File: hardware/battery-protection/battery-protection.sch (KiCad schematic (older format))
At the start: 20 parts, among them J1 M6 Battery input, J2 M5 Ground, J3 M5 Output, J4 M5 Output, J5 M5 Output, Q1 Q_PMOS_SGD, Q2 Q_PMOS_SGD, Q3 Q_PMOS_SGD, Q4 Q_PMOS_SGD, Q5 Q_PMOS_SGD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

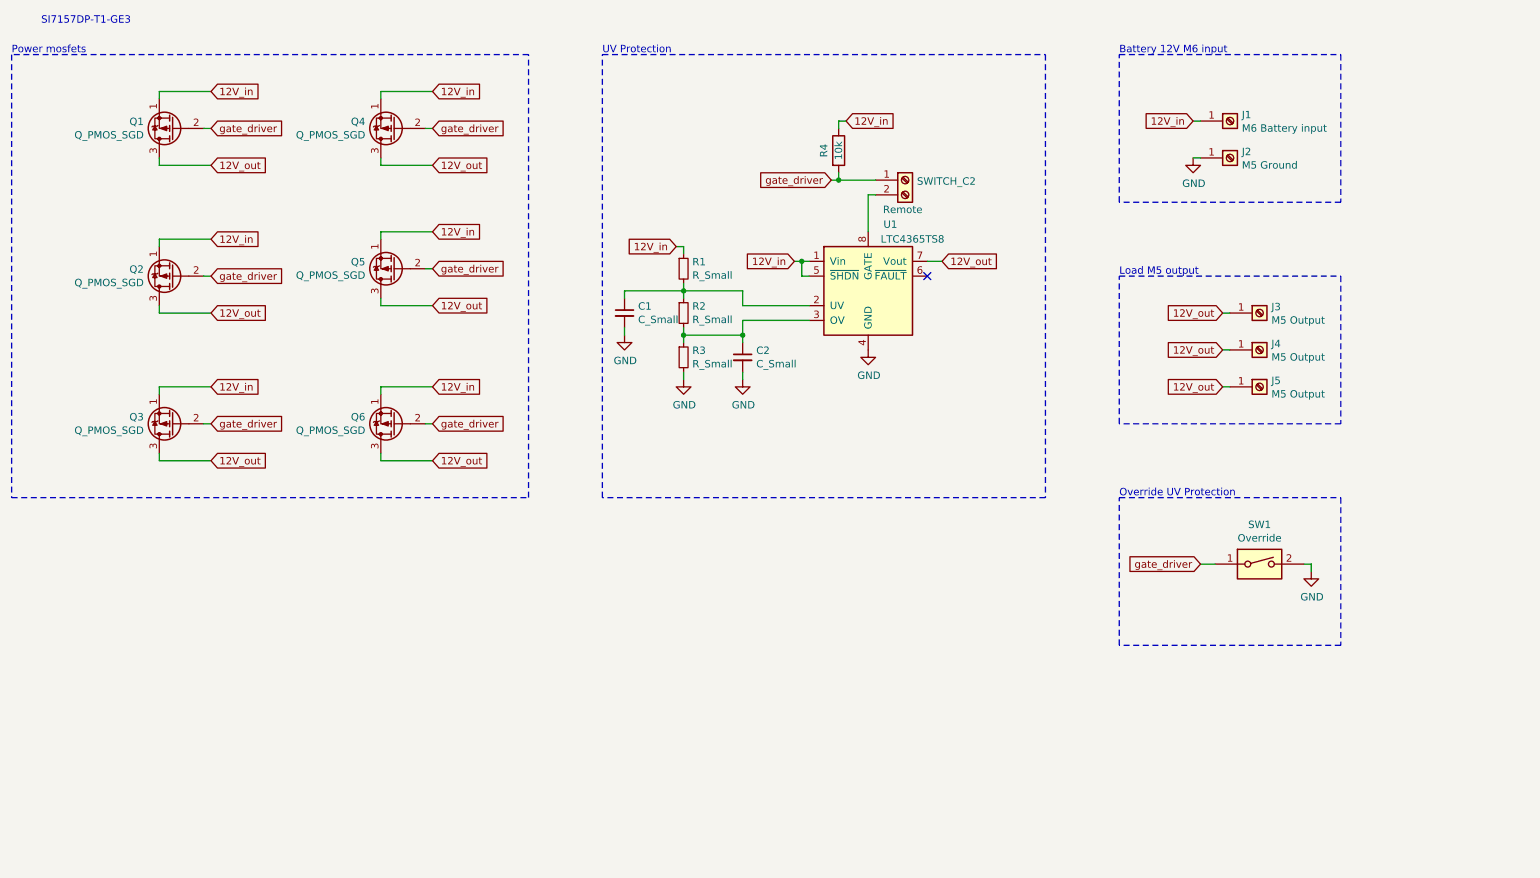
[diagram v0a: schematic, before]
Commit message: Finished routing battery protection
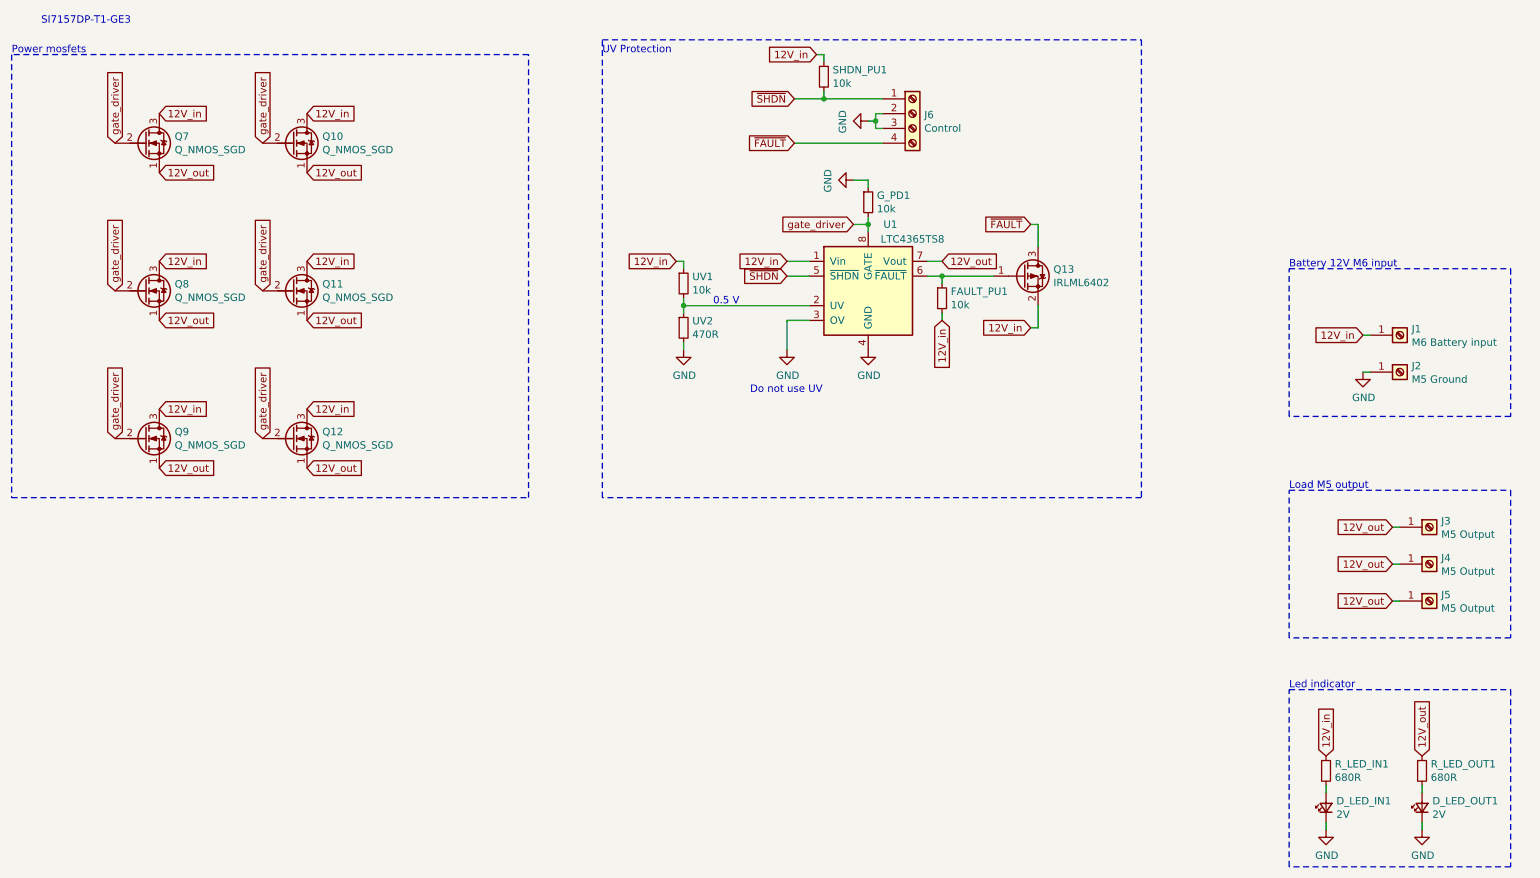
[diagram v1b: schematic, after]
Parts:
- removed C1, C2: C_Small, Capacitor_SMD:C_0603_1608Metric, symbol Device:C_Small
- removed Q1, Q2, Q3, Q4, Q5, Q6: Q_PMOS_SGD, mosfet:POWERPAKSO-8, symbol Device:Q_PMOS_SGD
- removed R3: R_Small, Resistor_SMD:R_0603_1608Metric, symbol Device:R_Small
- removed R4: 10k, Resistor_SMD:R_0603_1608Metric, symbol Device:R
- removed SW1: Override, symbol Switch:SW_DIP_x01
- removed SWITCH_C2: Remote, TerminalBlock_Phoenix:TerminalBlock_Phoenix_PT-1,5-2-5.0-H_1x02_P5.00mm_Horizontal, symbol Connector:Screw_Terminal_01x02
- added D_LED_IN1, D_LED_OUT1: 2V, LED_SMD:LED_0603_1608Metric, symbol Device:LED_Small
- added FAULT_PU1, G_PD1, SHDN_PU1: 10k, Resistor_SMD:R_0603_1608Metric, symbol Device:R_Small
- added J6: Control, TerminalBlock_Phoenix:TerminalBlock_Phoenix_MKDS-1,5-4_1x04_P5.00mm_Horizontal, symbol Connector:Screw_Terminal_01x04
- added Q10, Q11, Q12, Q7, Q8, Q9: Q_NMOS_SGD, mosfet:SQJA72EPT1_GE3, symbol Device:Q_NMOS_SGD
- added Q13: IRLML6402, Package_TO_SOT_SMD:SOT-23, symbol Transistor_FET:IRLML6402
- added R_LED_IN1, R_LED_OUT1: 680R, Resistor_SMD:R_0603_1608Metric, symbol Device:R_Small
- U1: footprint (none) -> Package_TO_SOT_SMD:SOT-23-8
- UV1: renamed from R1; value R_Small -> 10k
- UV2: renamed from R2; value R_Small -> 470R
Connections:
- net 12V_in: now also FAULT_PU1.2, Q10.3 (D), Q11.3 (D), Q12.3 (D), Q13.2 (S), Q7.3 (D), Q8.3 (D), Q9.3 (D), R_LED_IN1.1, SHDN_PU1.1; no longer U1.5 (~SHDN)
- net 12V_out: now also Q10.1 (S), Q11.1 (S), Q12.1 (S), Q7.1 (S), Q8.1 (S), Q9.1 (S), R_LED_OUT1.1
- net GND: now also U1.3 (OV), UV2.2, D_LED_IN1.1 (K), D_LED_OUT1.1 (K), G_PD1.1, J6.2 (Pin_2), J6.3 (Pin_3)
- net gate_driver: now also U1.8 (GATE), G_PD1.2, Q10.2 (G), Q11.2 (G), Q12.2 (G), Q7.2 (G), Q8.2 (G), Q9.2 (G)
- net at U1.6 (~FAULT): now also FAULT_PU1.1, Q13.1 (G)
- new net: D_LED_IN1.2 (A), R_LED_IN1.2
- new net: D_LED_OUT1.2 (A), R_LED_OUT1.2
- new net ~FAULT: J6.4 (Pin_4), Q13.3 (D)
- new net ~SHDN: J6.1 (Pin_1), SHDN_PU1.2, U1.5 (~SHDN)
- no-connect marks 1 -> 0
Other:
- note added: "0.5 V"
- note added: "Do not use UV"
- note added: "Led indicator"
- note removed: "Override UV Protection"
- moved on the sheet: J1, J2, J3, J4, J5, UV1, UV2

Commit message: Changed to pd for mcu and added pinout for led
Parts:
- removed FAULT_PU1, SHDN_PU1: 10k, Resistor_SMD:R_0603_1608Metric, symbol Device:R_Small
- removed J6: Control, TerminalBlock_Phoenix:TerminalBlock_Phoenix_MKDS-1,5-4_1x04_P5.00mm_Horizontal, symbol Connector:Screw_Terminal_01x04
- removed Q13: IRLML6402, Package_TO_SOT_SMD:SOT-23, symbol Transistor_FET:IRLML6402
- added J6: CTRL, TerminalBlock_Phoenix:TerminalBlock_Phoenix_MKDS-1,5-6_1x06_P5.00mm_Horizontal, symbol Connector:Screw_Terminal_01x06
- added SHDN_PD1: 10k, Resistor_SMD:R_0603_1608Metric, symbol Device:R_Small
- added UV3: 100pF, Capacitor_SMD:C_0603_1608Metric, symbol Device:C_Small
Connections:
- net 12V_in: now also J6.1 (Pin_1), J6.3 (Pin_3)
- net 12V_out: now also J6.5 (Pin_5)
- net GND: now also J6.4 (Pin_4), J6.6 (Pin_6), SHDN_PD1.2, UV3.2
- net ~SHDN: now also J6.2 (Pin_2), SHDN_PD1.1
- net at U1.2 (UV), UV1.2, UV2.1: now also UV3.1
- no-connect marks 0 -> 1
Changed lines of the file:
@@
 SI7157DP-T1-GE3
-$Comp
-L power:GND #PWR0107
-U 1 1 5F04D66F
-P 6800 1450
-F 0 "#PWR0107" H 6800 1200 50  0001 C CNN
-F 1 "GND" H 6805 1277 50  0000 C CNN
-F 2 "" H 6800 1450 50  0001 C CNN
-F 3 "" H 6800 1450 50  0001 C CNN
-	1    6800 1450
-	0    1    1    0
-$EndComp
 $Comp
 L Device:R_Small R_LED_IN1
@@
 Wire Wire Line
 	6250 2400 6400 2400
-Text GLabel 6300 1300 0    50   Input ~ 0
+Text GLabel 6750 1200 0    50   Input ~ 0
 ~SHDN
-$Comp
-L Device:R_Small SHDN_PU1
-U 1 1 5F053F2F
-P 6500 1150
-F 0 "SHDN_PU1" H 6559 1196 50  0000 L CNN
-F 1 "10k" H 6559 1105 50  0000 L CNN
-F 2 "Resistor_SMD:R_0603_1608Metric" H 6500 1150 50  0001 C CNN
-F 3 "~" H 6500 1150 50  0001 C CNN
-	1    6500 1150
-	1    0    0    -1
-$EndComp
-Text GLabel 6450 1000 0    50   Input ~ 0
-12V_in
-Wire Wire Line
-	6450 1000 6500 1000
-Wire Wire Line
-	6500 1000 6500 1050
-Wire Wire Line
-	6300 1300 6500 1300
-Wire Wire Line
-	6500 1300 6500 1250
-Wire Wire Line
-	6900 1300 6500 1300
-Connection ~ 6500 1300
+Wire Wire Line
+	6750 1200 7050 1200
 Text GLabel 6700 2150 0    50   Input ~ 0
 gate_driver
@@
 	0    1    1    0
 $EndComp
-Text GLabel 6300 1600 0    50   Input ~ 0
-~FAULT
-Wire Wire Line
-	6300 1600 6900 1600
-$Comp
-L Transistor_FET:IRLML6402 Q13
-U 1 1 5F068DCD
-P 7850 2500
-F 0 "Q13" H 8054 2546 50  0000 L CNN
-F 1 "IRLML6402" H 8054 2455 50  0000 L CNN
-F 2 "Package_TO_SOT_SMD:SOT-23" H 8050 2425 50  0001 L CIN
-F 3 "https://www.infineon.com/dgdl/irlml6402pbf.pdf?fileId=5546d462533600a401535668d5c2263c" H 7850 2500 50  0001 L CNN
-	1    7850 2500
-	1    0    0    -1
-$EndComp
-Wire Wire Line
-	7200 2500 7300 2500
-Text GLabel 7900 2150 0    50   Input ~ 0
-~FAULT
-Text GLabel 7900 2850 0    50   Input ~ 0
-12V_in
-$Comp
-L Connector:Screw_Terminal_01x04 J6
-U 1 1 5F06C597
-P 7100 1400
-F 0 "J6" H 7180 1392 50  0000 L CNN
-F 1 "Control" H 7180 1301 50  0000 L CNN
-F 2 "TerminalBlock_Phoenix:TerminalBlock_Phoenix_MKDS-1,5-4_1x04_P5.00mm_Horizontal" H 7100 1400 50  0001 C CNN
-F 3 "~" H 7100 1400 50  0001 C CNN
-	1    7100 1400
-	1    0    0    -1
-$EndComp
-$Comp
-L Device:R_Small FAULT_PU1
-U 1 1 5F06D302
-P 7300 2650
-F 0 "FAULT_PU1" H 7359 2696 50  0000 L CNN
-F 1 "10k" H 7359 2605 50  0000 L CNN
-F 2 "Resistor_SMD:R_0603_1608Metric" H 7300 2650 50  0001 C CNN
-F 3 "~" H 7300 2650 50  0001 C CNN
-	1    7300 2650
-	1    0    0    -1
-$EndComp
-Text GLabel 7300 2800 3    50   Input ~ 0
-12V_in
-Wire Wire Line
-	7300 2800 7300 2750
-Wire Wire Line
-	7300 2550 7300 2500
-Connection ~ 7300 2500
-Wire Wire Line
-	7300 2500 7650 2500
-Wire Wire Line
-	6800 1450 6850 1450
-Wire Wire Line
-	6850 1450 6850 1400
-Wire Wire Line
-	6850 1400 6900 1400
-Wire Wire Line
-	6900 1500 6850 1500
-Wire Wire Line
-	6850 1500 6850 1450
-Connection ~ 6850 1450
-Wire Wire Line
-	7900 2850 7950 2850
-Wire Wire Line
-	7950 2850 7950 2700
-Wire Wire Line
-	7950 2300 7950 2150
-Wire Wire Line
-	7950 2150 7900 2150
 Wire Wire Line
 	6400 2800 6250 2800
@@
 	5550 2650 5550 2700
 Wire Wire Line
-	6400 2700 5550 2700
+	6400 2700 5900 2700
 Connection ~ 5550 2700
 Wire Wire Line
@@
 Text Notes 6000 3300 0    50   ~ 0
 Do not use UV
+Connection ~ 7050 1200
+Wire Wire Line
+	7050 1200 8050 1200
+$Comp
+L Device:R_Small SHDN_PD1
+U 1 1 5F22E95E
+P 7050 1350
+F 0 "SHDN_PD1" H 7109 1396 50  0000 L CNN
+F 1 "10k" H 7109 1305 50  0000 L CNN
+F 2 "Resistor_SMD:R_0603_1608Metric" H 7050 1350 50  0001 C CNN
+F 3 "~" H 7050 1350 50  0001 C CNN
+	1    7050 1350
+	1    0    0    -1
+$EndComp
+Wire Wire Line
+	7050 1250 7050 1200
+$Comp
+L power:GND #PWR0105
+U 1 1 5F22F7EF
+P 7050 1500
+F 0 "#PWR0105" H 7050 1250 50  0001 C CNN
+F 1 "GND" H 7055 1327 50  0000 C CNN
+F 2 "" H 7050 1500 50  0001 C CNN
+F 3 "" H 7050 1500 50  0001 C CNN
+	1    7050 1500
+	1    0    0    -1
+$EndComp
+Wire Wire Line
+	7050 1500 7050 1450
+$Comp
+L Device:C_Small UV3
+U 1 1 5F23BE67
+P 5900 2850
+F 0 "UV3" H 5992 2896 50  0000 L CNN
+F 1 "100pF" H 5992 2805 50  0000 L CNN
+F 2 "Capacitor_SMD:C_0603_1608Metric" H 5900 2850 50  0001 C CNN
+F 3 "~" H 5900 2850 50  0001 C CNN
+	1    5900 2850
+	1    0    0    -1
+$EndComp
+$Comp
+L power:GND #PWR0111
+U 1 1 5F23C362
+P 5900 3000
+F 0 "#PWR0111" H 5900 2750 50  0001 C CNN
+F 1 "GND" H 5905 2827 50  0000 C CNN
+F 2 "" H 5900 3000 50  0001 C CNN
+F 3 "" H 5900 3000 50  0001 C CNN
+	1    5900 3000
+	1    0    0    -1
+$EndComp
+Wire Wire Line
+	5900 3000 5900 2950
+Wire Wire Line
+	5900 2750 5900 2700
+Connection ~ 5900 2700
+Wire Wire Line
+	5900 2700 5550 2700
+NoConn ~ 7200 2500
+$Comp
+L Connector:Screw_Terminal_01x06 J6
+U 1 1 5F269231
+P 8250 1300
+F 0 "J6" H 8330 1292 50  0000 L CNN
+F 1 "CTRL" H 8330 1201 50  0000 L CNN
+F 2 "TerminalBlock_Phoenix:TerminalBlock_Phoenix_MKDS-1,5-6_1x06_P5.00mm_Horizontal" H 8250 1300 50  0001 C CNN
+F 3 "~" H 8250 1300 50  0001 C CNN
+	1    8250 1300
+	1    0    0    -1
+$EndComp
+Wire Wire Line
+	7950 1100 8050 1100
+Text GLabel 7950 1100 0    50   Input ~ 0
+12V_in
+Text GLabel 7950 1300 0    50   Input ~ 0
+12V_in
+Text GLabel 7950 1500 0    50   Input ~ 0
+12V_out
+Wire Wire Line
+	7550 1600 8050 1600
+Wire Wire Line
+	7950 1500 8050 1500
+Wire Wire Line
+	8050 1300 7950 1300
+Wire Wire Line
+	7550 1600 7550 1400
+Wire Wire Line
+	7550 1400 8050 1400
+Wire Wire Line
+	7550 1600 7550 1650
+Connection ~ 7550 1600
+$Comp
+L power:GND #PWR0107
+U 1 1 5F26DF10
+P 7550 1650
+F 0 "#PWR0107" H 7550 1400 50  0001 C CNN
+F 1 "GND" H 7555 1477 50  0000 C CNN
+F 2 "" H 7550 1650 50  0001 C CNN
+F 3 "" H 7550 1650 50  0001 C CNN
+	1    7550 1650
+	1    0    0    -1
+$EndComp
 $EndSCHEMATC

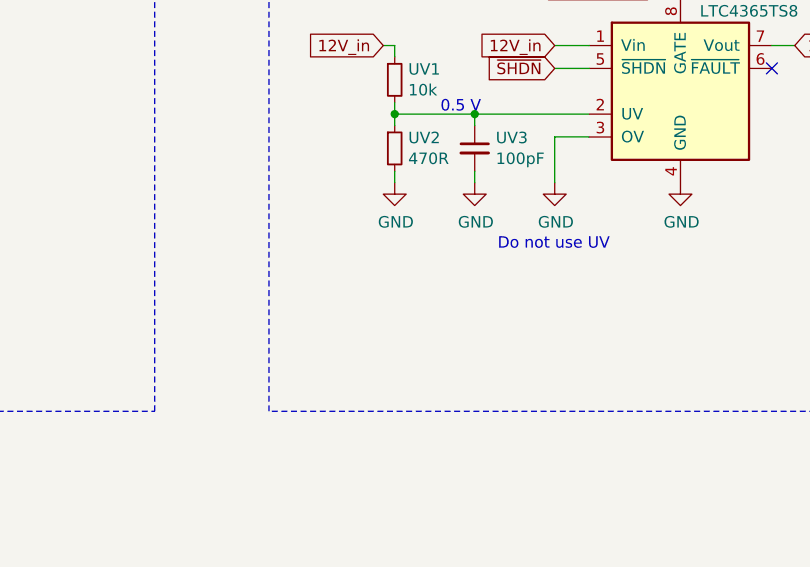
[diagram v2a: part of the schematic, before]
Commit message: Changed UV resistor value
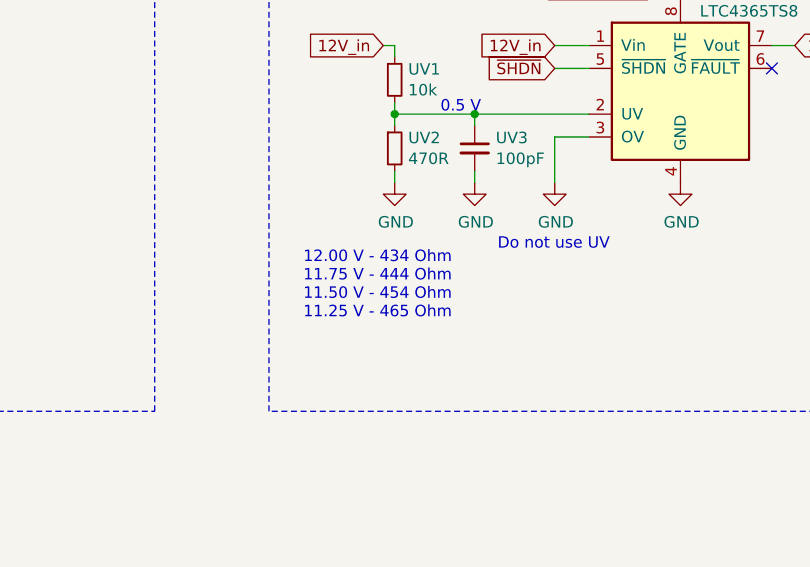
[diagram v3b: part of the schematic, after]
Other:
- note added: "12.00 V - 434 Ohm\n11.75 V - 444 Ohm\n11.50 V - 454 Ohm\n11.25 V - 465 Ohm"
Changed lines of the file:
@@
 	1    0    0    -1
 $EndComp
+Text Notes 5150 3600 0    50   ~ 0
+12.00 V - 434 Ohm\n11.75 V - 444 Ohm\n11.50 V - 454 Ohm\n11.25 V - 465 Ohm
 $EndSCHEMATC
